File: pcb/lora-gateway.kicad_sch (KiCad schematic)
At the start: 6 parts, among them J1 USB_B_Micro, J2 Conn_01x06, J3 Conn_01x06, J4 Conn_Coaxial, U1 RFM95W-868S2, U2 ATmega2560-16A

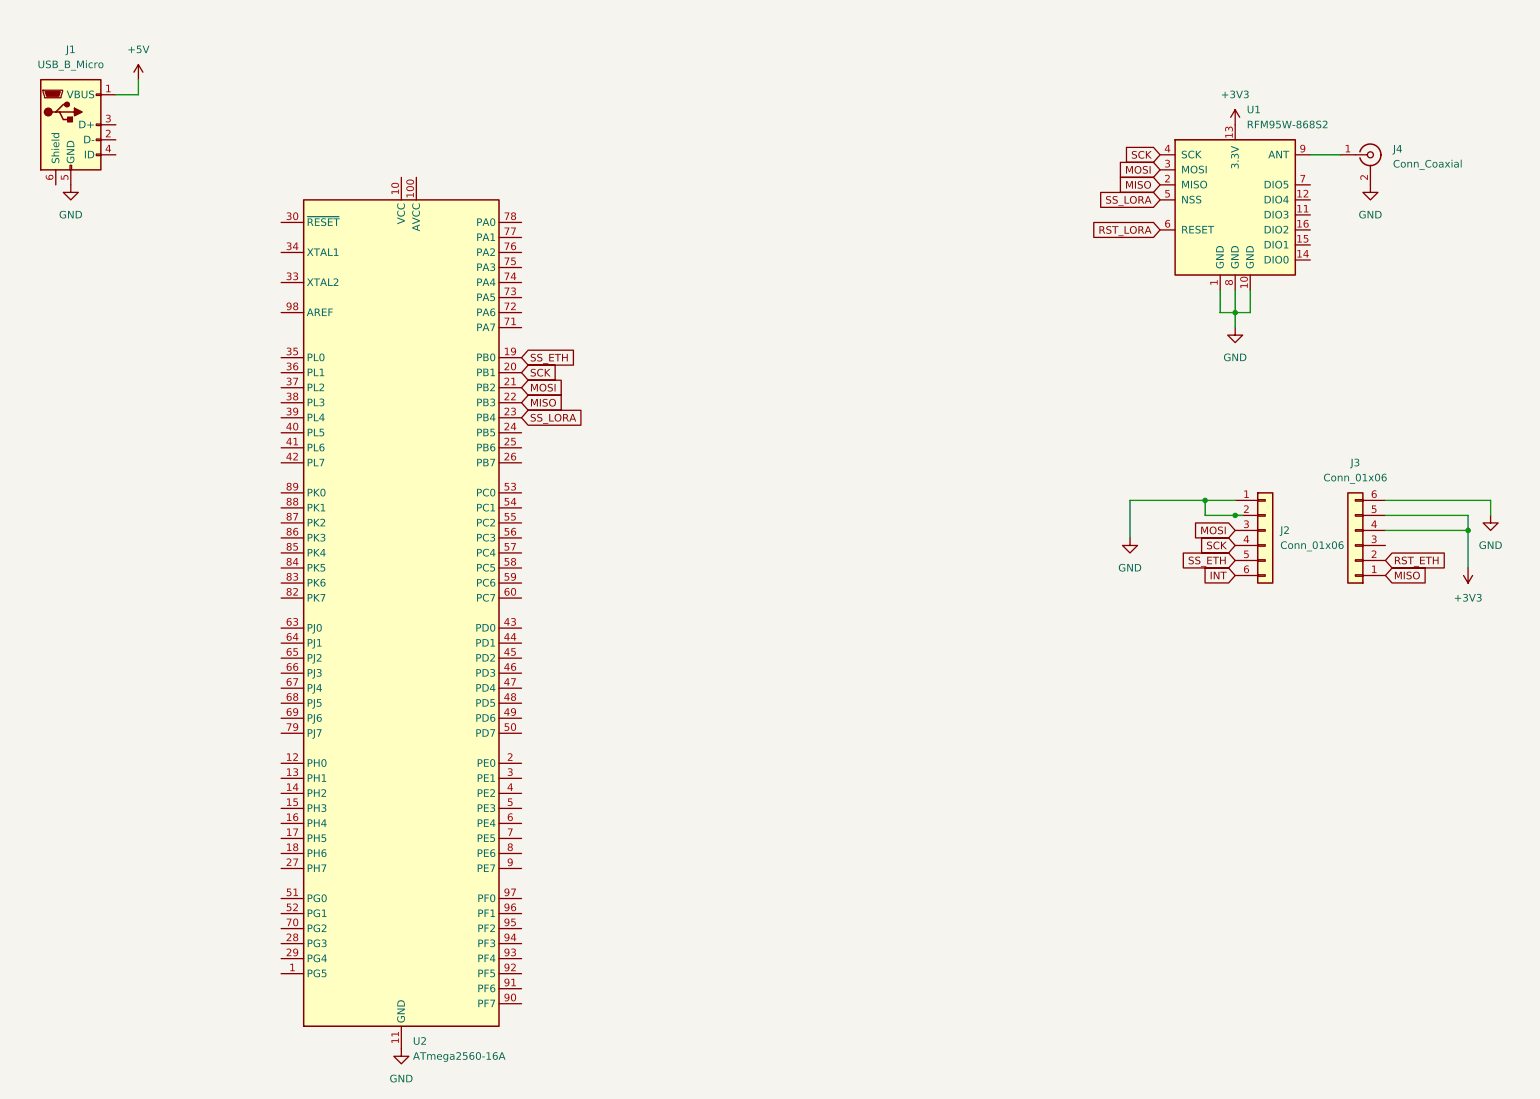
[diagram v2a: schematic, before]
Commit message: add regulator
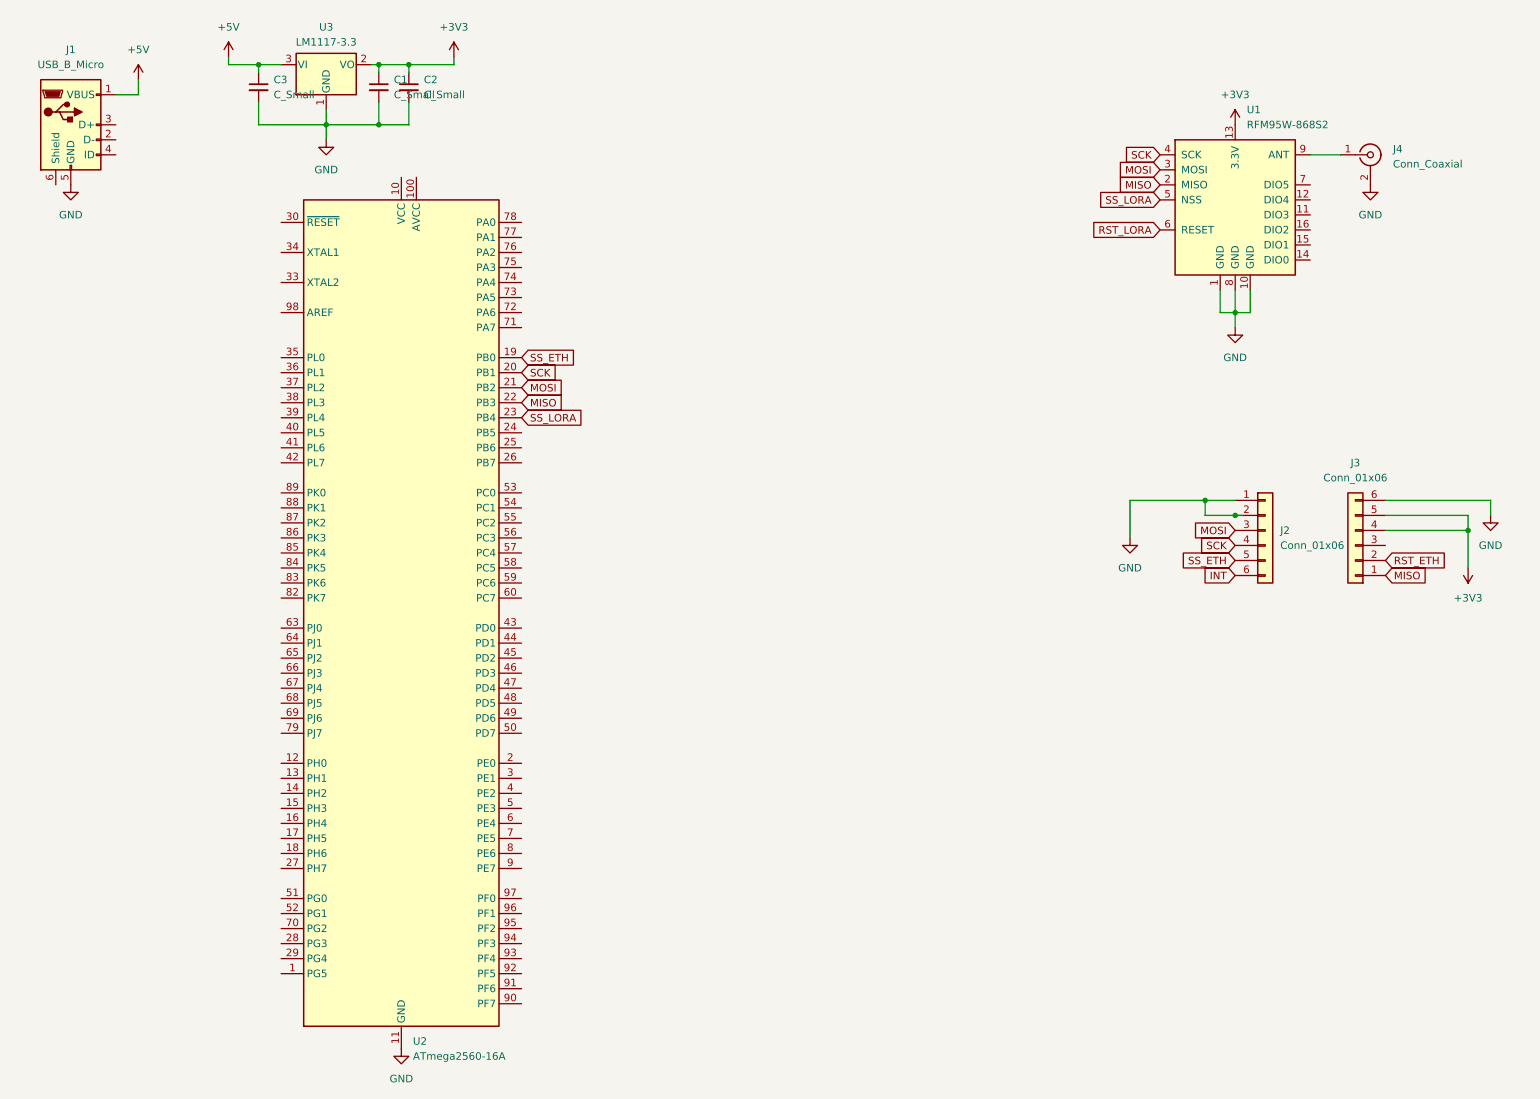
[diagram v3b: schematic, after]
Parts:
- added C1, C2, C3: C_Small, Capacitor_SMD:C_0603_1608Metric, symbol Device:C_Small
- added U3: LM1117-3.3, Package_TO_SOT_SMD:SOT-223-3_TabPin2, symbol Regulator_Linear:LM1117-3.3
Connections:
- net +3V3: now also C1.1, C2.1, U3.2 (VO)
- net +5V: now also C3.1, U3.3 (VI)
- net GND: now also C1.2, C2.2, C3.2, U3.1 (GND)
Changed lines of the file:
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@@
 (kicad_sch (version 20230121) (generator eeschema)
   (paper "A4")
+  (junction (at 74.93 30.48) (diameter 0) (color 0 0 0 0)
+  )
+  (junction (at 214.63 93.98) (diameter 0) (color 0 0 0 0)
+  )
+  (junction (at 66.04 30.48) (diameter 0) (color 0 0 0 0)
+  )
+  (junction (at 219.71 62.23) (diameter 0) (color 0 0 0 0)
+  )
   (junction (at 219.71 96.52) (diameter 0) (color 0 0 0 0)
   )
-  (junction (at 214.63 93.98) (diameter 0) (color 0 0 0 0)
-  )
-  (junction (at 219.71 62.23) (diameter 0) (color 0 0 0 0)
-  )
   (junction (at 259.08 99.06) (diameter 0) (color 0 0 0 0)
   )
+  (junction (at 80.01 20.32) (diameter 0) (color 0 0 0 0)
+  )
+  (junction (at 74.93 20.32) (diameter 0) (color 0 0 0 0)
+  )
+  (junction (at 54.61 20.32) (diameter 0) (color 0 0 0 0)
+  )
   (wire (pts (xy 219.71 62.23) (xy 222.25 62.23))
     (stroke (width 0) (type default))
@@
     (stroke (width 0) (type default))
   )
-  (wire (pts (xy 219.71 96.52) (xy 214.63 96.52))
+  (wire (pts (xy 80.01 26.67) (xy 80.01 30.48))
     (stroke (width 0) (type default))
   )
@@
     (stroke (width 0) (type default))
   )
+  (wire (pts (xy 66.04 27.94) (xy 66.04 30.48))
+    (stroke (width 0) (type default))
+  )
   (wire (pts (xy 219.71 93.98) (xy 214.63 93.98))
     (stroke (width 0) (type default))
@@
     (stroke (width 0) (type default))
   )
+  (wire (pts (xy 49.53 20.32) (xy 54.61 20.32))
+    (stroke (width 0) (type default))
+  )
+  (wire (pts (xy 54.61 26.67) (xy 54.61 30.48))
+    (stroke (width 0) (type default))
+  )
+  (wire (pts (xy 49.53 19.05) (xy 49.53 20.32))
+    (stroke (width 0) (type default))
+  )
+  (wire (pts (xy 74.93 20.32) (xy 74.93 21.59))
+    (stroke (width 0) (type default))
+  )
   (wire (pts (xy 201.93 93.98) (xy 201.93 100.33))
     (stroke (width 0) (type default))
   )
+  (wire (pts (xy 73.66 20.32) (xy 74.93 20.32))
+    (stroke (width 0) (type default))
+  )
+  (wire (pts (xy 219.71 96.52) (xy 220.98 96.52))
+    (stroke (width 0) (type default))
+  )
   (wire (pts (xy 245.11 93.98) (xy 262.89 93.98))
     (stroke (width 0) (type default))
   )
-  (wire (pts (xy 220.98 96.52) (xy 219.71 96.52))
+  (wire (pts (xy 214.63 96.52) (xy 219.71 96.52))
+    (stroke (width 0) (type default))
+  )
+  (wire (pts (xy 54.61 20.32) (xy 54.61 21.59))
     (stroke (width 0) (type default))
   )
@@
     (stroke (width 0) (type default))
   )
+  (wire (pts (xy 74.93 20.32) (xy 80.01 20.32))
+    (stroke (width 0) (type default))
+  )
+  (wire (pts (xy 80.01 20.32) (xy 80.01 21.59))
+    (stroke (width 0) (type default))
+  )
+  (wire (pts (xy 74.93 30.48) (xy 66.04 30.48))
+    (stroke (width 0) (type default))
+  )
+  (wire (pts (xy 87.63 19.05) (xy 87.63 20.32))
+    (stroke (width 0) (type default))
+  )
   (wire (pts (xy 34.29 25.4) (xy 34.29 22.86))
     (stroke (width 0) (type default))
   )
+  (wire (pts (xy 54.61 20.32) (xy 58.42 20.32))
+    (stroke (width 0) (type default))
+  )
   (wire (pts (xy 219.71 58.42) (xy 219.71 62.23))
     (stroke (width 0) (type default))
@@
     (stroke (width 0) (type default))
   )
+  (wire (pts (xy 80.01 20.32) (xy 87.63 20.32))
+    (stroke (width 0) (type default))
+  )
   (wire (pts (xy 232.41 35.56) (xy 237.49 35.56))
     (stroke (width 0) (type default))
   )
+  (wire (pts (xy 66.04 30.48) (xy 66.04 33.02))
+    (stroke (width 0) (type default))
+  )
   (wire (pts (xy 217.17 62.23) (xy 219.71 62.23))
     (stroke (width 0) (type default))
   )
+  (wire (pts (xy 80.01 30.48) (xy 74.93 30.48))
+    (stroke (width 0) (type default))
+  )
   (wire (pts (xy 30.48 25.4) (xy 34.29 25.4))
     (stroke (width 0) (type default))
@@
     (stroke (width 0) (type default))
   )
+  (wire (pts (xy 54.61 30.48) (xy 66.04 30.48))
+    (stroke (width 0) (type default))
+  )
   (wire (pts (xy 245.11 99.06) (xy 259.08 99.06))
+    (stroke (width 0) (type default))
+  )
+  (wire (pts (xy 74.93 26.67) (xy 74.93 30.48))
     (stroke (width 0) (type default))
   )
@@
     )
   )
+  (symbol (lib_id "power:GND") (at 66.04 33.02 0) (unit 1)
+    (in_bom yes) (on_board yes) (dnp no) (fields_autoplaced)
+    (property "Reference" "#PWR011" (at 66.04 39.37 0)
+      (effects (font (size 1.27 1.27)) hide)
+    )
+    (property "Value" "GND" (at 66.04 38.1 0)
+      (effects (font (size 1.27 1.27)))
+    )
+    (property "Footprint" "" (at 66.04 33.02 0)
+      (effects (font (size 1.27 1.27)) hide)
+    )
+    (property "Datasheet" "" (at 66.04 33.02 0)
+      (effects (font (size 1.27 1.27)) hide)
+    )
+    (pin "1")
+    (instances
+      (project "lora-gateway"
+        (path "/5fd0eb65-7f10-4bbb-b642-b528dcb1ea0e"
+          (reference "#PWR011") (unit 1)
+        )
+      )
+    )
+  )
+  (symbol (lib_id "Device:C_Small") (at 54.61 24.13 0) (unit 1)
+    (in_bom yes) (on_board yes) (dnp no) (fields_autoplaced)
+    (property "Reference" "C3" (at 57.15 22.8663 0)
+      (effects (font (size 1.27 1.27)) (justify left))
+    )
+    (property "Value" "C_Small" (at 57.15 25.4063 0)
+      (effects (font (size 1.27 1.27)) (justify left))
+    )
+    (property "Footprint" "Capacitor_SMD:C_0603_1608Metric" (at 54.61 24.13 0)
+      (effects (font (size 1.27 1.27)) hide)
+    )
+    (property "Datasheet" "~" (at 54.61 24.13 0)
+      (effects (font (size 1.27 1.27)) hide)
+    )
+    (pin "1")
+    (pin "2")
+    (instances
+      (project "lora-gateway"
+        (path "/5fd0eb65-7f10-4bbb-b642-b528dcb1ea0e"
+          (reference "C3") (unit 1)
+        )
+      )
+    )
+  )
   (symbol (lib_name "GND_1") (lib_id "power:GND") (at 201.93 100.33 0) (unit 1)
     (in_bom yes) (on_board yes) (dnp no) (fields_autoplaced)
@@
     )
   )
+  (symbol (lib_id "Device:C_Small") (at 80.01 24.13 0) (unit 1)
+    (in_bom yes) (on_board yes) (dnp no) (fields_autoplaced)
+    (property "Reference" "C2" (at 82.55 22.8663 0)
+      (effects (font (size 1.27 1.27)) (justify left))
+    )
+    (property "Value" "C_Small" (at 82.55 25.4063 0)
+      (effects (font (size 1.27 1.27)) (justify left))
+    )
+    (property "Footprint" "Capacitor_SMD:C_0603_1608Metric" (at 80.01 24.13 0)
+      (effects (font (size 1.27 1.27)) hide)
+    )
+    (property "Datasheet" "~" (at 80.01 24.13 0)
+      (effects (font (size 1.27 1.27)) hide)
+    )
+    (pin "1")
+    (pin "2")
+    (instances
+      (project "lora-gateway"
+        (path "/5fd0eb65-7f10-4bbb-b642-b528dcb1ea0e"
+          (reference "C2") (unit 1)
+        )
+      )
+    )
+  )
   (symbol (lib_id "Connector_Generic:Conn_01x06") (at 240.03 101.6 180) (unit 1)
     (in_bom yes) (on_board yes) (dnp no) (fields_autoplaced)
@@
     )
   )
+  (symbol (lib_id "Regulator_Linear:LM1117-3.3") (at 66.04 20.32 0) (unit 1)
+    (in_bom yes) (on_board yes) (dnp no) (fields_autoplaced)
+    (property "Reference" "U3" (at 66.04 13.97 0)
+      (effects (font (size 1.27 1.27)))
+    )
+    (property "Value" "LM1117-3.3" (at 66.04 16.51 0)
+      (effects (font (size 1.27 1.27)))
+    )
+    (property "Footprint" "Package_TO_SOT_SMD:SOT-223-3_TabPin2" (at 66.04 20.32 0)
+      (effects (font (size 1.27 1.27)) hide)
+    )
+    (property "Datasheet" "http://www.ti.com/lit/ds/symlink/lm1117.pdf" (at 66.04 20.32 0)
+      (effects (font (size 1.27 1.27)) hide)
+    )
+    (pin "1")
+    (pin "2")
+    (pin "3")
+    (instances
+      (project "lora-gateway"
+        (path "/5fd0eb65-7f10-4bbb-b642-b528dcb1ea0e"
+          (reference "U3") (unit 1)
+        )
+      )
+    )
+  )
+  (symbol (lib_id "Device:C_Small") (at 74.93 24.13 0) (unit 1)
+    (in_bom yes) (on_board yes) (dnp no) (fields_autoplaced)
+    (property "Reference" "C1" (at 77.47 22.8663 0)
+      (effects (font (size 1.27 1.27)) (justify left))
+    )
+    (property "Value" "C_Small" (at 77.47 25.4063 0)
+      (effects (font (size 1.27 1.27)) (justify left))
+    )
+    (property "Footprint" "Capacitor_SMD:C_0603_1608Metric" (at 74.93 24.13 0)
+      (effects (font (size 1.27 1.27)) hide)
+    )
+    (property "Datasheet" "~" (at 74.93 24.13 0)
+      (effects (font (size 1.27 1.27)) hide)
+    )
+    (pin "1")
+    (pin "2")
+    (instances
+      (project "lora-gateway"
+        (path "/5fd0eb65-7f10-4bbb-b642-b528dcb1ea0e"
+          (reference "C1") (unit 1)
+        )
+      )
+    )
+  )
   (symbol (lib_id "power:+5V") (at 34.29 22.86 0) (unit 1)
     (in_bom yes) (on_board yes) (dnp no) (fields_autoplaced)
@@
     )
   )
+  (symbol (lib_id "power:+5V") (at 49.53 19.05 0) (unit 1)
+    (in_bom yes) (on_board yes) (dnp no) (fields_autoplaced)
+    (property "Reference" "#PWR010" (at 49.53 22.86 0)
+      (effects (font (size 1.27 1.27)) hide)
+    )
+    (property "Value" "+5V" (at 49.53 13.97 0)
+      (effects (font (size 1.27 1.27)))
+    )
+    (property "Footprint" "" (at 49.53 19.05 0)
+      (effects (font (size 1.27 1.27)) hide)
+    )
+    (property "Datasheet" "" (at 49.53 19.05 0)
+      (effects (font (size 1.27 1.27)) hide)
+    )
+    (pin "1")
+    (instances
+      (project "lora-gateway"
+        (path "/5fd0eb65-7f10-4bbb-b642-b528dcb1ea0e"
+          (reference "#PWR010") (unit 1)
+        )
+      )
+    )
+  )
   (symbol (lib_name "GND_1") (lib_id "power:GND") (at 262.89 96.52 0) (unit 1)
     (in_bom yes) (on_board yes) (dnp no) (fields_autoplaced)
@@
         )
       )
+    )
+  )
+  (symbol (lib_id "power:+3V3") (at 87.63 19.05 0) (unit 1)
+    (in_bom yes) (on_board yes) (dnp no) (fields_autoplaced)
+    (property "Reference" "#PWR012" (at 87.63 22.86 0)
+      (effects (font (size 1.27 1.27)) hide)
+    )
+    (property "Value" "+3V3" (at 87.63 13.97 0)
+      (effects (font (size 1.27 1.27)))
+    )
+    (property "Footprint" "" (at 87.63 19.05 0)
+      (effects (font (size 1.27 1.27)) hide)
+    )
+    (property "Datasheet" "" (at 87.63 19.05 0)
+      (effects (font (size 1.27 1.27)) hide)
+    )
+    (pin "1")
+    (instances
+      (project "lora-gateway"
+        (path "/5fd0eb65-7f10-4bbb-b642-b528dcb1ea0e"
+          (reference "#PWR012") (unit 1)
+        )
+      )
